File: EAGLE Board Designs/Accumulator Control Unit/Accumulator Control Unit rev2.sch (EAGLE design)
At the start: 215 parts, among them J1 CONNECTOR-CAN_μF_S_RA_, J2 CONNECTOR-8_MF_T_V_, J3 CONNECTOR-8_FS_S, J4 CONNECTOR-2_MF_T_V_, J5 CONNECTOR-12_MF_T_V_, J6 CONNECTOR-14_MF_T_V_, Q1 TRANSISTOR_N_MOS__PMV15ENEA, Q2 TRANSISTOR_N_MOS__PMV15ENEA, Q3 TRANSISTOR_N_MOS__PMV15ENEA, Q4 TRANSISTOR_N_MOS__PMV15ENEA, T1 TRANSFORMER_HM2112ZNLT_AIRGAP, U1 RELAY_SOLIDSTATE_NO, U10 OPAMP_1_CHANNEL_OPA991, U11 LOGICGATE_AND_DCK3, U12 OPAMP_1_CHANNEL_OPA991, U13 OPAMP_1_CHANNEL_OPA991, U14 OPAMP_1_CHANNEL_OPA991, U15 LOGICGATE_AND_DCK3, U16 RELAY_SOLIDSTATE_NO, U17 VOLTAGE_REGULATOR_SOT223_3.3V, U18 OPAMP_1_CHANNEL_OPA991, U19 MAX7404, U2 ADG1423, U20 OPAMP_1_CHANNEL_OPA991, U21 LOGICGATE_BUFFER, U22 OPAMP_1_CHANNEL_OPA991, U25 TCAN1051HQV-Q1, U26 MAX7404, U27 OPAMP_1_CHANNEL_OPA991, U28 MAX7404, U29 OPAMP_1_CHANNEL_OPA991, U3 LM555, U30 MAX7404, U4 OPAMP_1_CHANNEL_OPA991, U40 RELAY_SOLIDSTATE_NO, U5 LTC6820, U6 ADM8316WBX30, U7 OPAMP_1_CHANNEL_OPA991, U8 LOGICGATE_AND_DCK3, U9 OPAMP_1_CHANNEL_OPA991

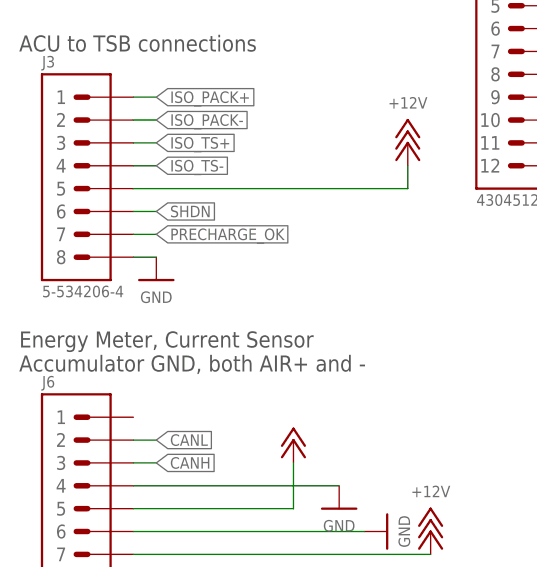
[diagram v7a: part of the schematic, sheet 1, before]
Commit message: added silkscreen
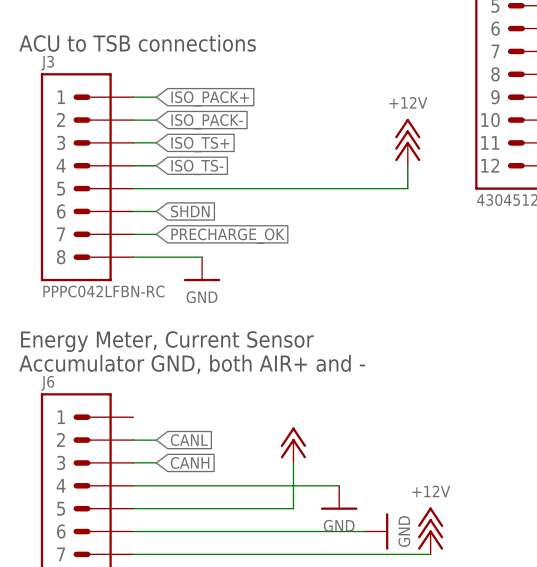
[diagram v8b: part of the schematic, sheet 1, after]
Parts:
- J3: value CONNECTOR-8_FS_S -> CONNECTOR-8_S_S; device HyTechDevices:CONNECTOR-8_FS_S -> HyTechDevices:CONNECTOR-8_S_S
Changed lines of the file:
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@@
 <part name="FRAME2" library="HyTechFrames" deviceset="FRAME" device=""/>
 <part name="FRAME4" library="HyTechFrames" deviceset="FRAME" device=""/>
-<part name="J3" library="HyTechDevices" deviceset="CONNECTOR-8_?_*" device="FS" technology="S"/>
+<part name="J3" library="HyTechDevices" deviceset="CONNECTOR-8_?_*" device="S" technology="S"/>
 <part name="P1" library="HyTechSupplies" deviceset="+12V" device=""/>
 <part name="P2" library="HyTechSupplies" deviceset="GND" device=""/>
@@
 <attribute name="RESISTANCE" x="255.27" y="113.03" size="1.27" layer="96" rot="R180" align="top-center"/>
 </instance>
-<instance part="P5" gate="1" x="22.86" y="144.78" smashed="yes">
-<attribute name="VALUE" x="22.86" y="143.51" size="1.27" layer="96" align="top-center"/>
+<instance part="P5" gate="1" x="27.94" y="144.78" smashed="yes">
+<attribute name="VALUE" x="27.94" y="143.51" size="1.27" layer="96" align="top-center"/>
 </instance>
 <instance part="J1" gate="G$1" x="10.16" y="195.58" smashed="yes">
@@
 <segment>
 <pinref part="P5" gate="1" pin="GND"/>
-<wire x1="22.86" y1="147.32" x2="20.32" y2="147.32" width="0.1524" layer="91"/>
+<wire x1="27.94" y1="147.32" x2="20.32" y2="147.32" width="0.1524" layer="91"/>
 <pinref part="J3" gate="G$1" pin="8"/>
 </segment>
